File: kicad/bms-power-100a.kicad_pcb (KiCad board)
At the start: 4 copper layers, 120 x 65 mm, 68 parts, among them J1 Conn_01x06, J2 Conn_01x06, P1 CONN_01X01, P2 CONN_01X01, P3 CONN_01X01, P4 CONN_01X01, Q1 IPT015N10N5, Q10 BSS123N, Q2 IPT015N10N5, Q21 ZXMP6A13F, Q3 IPT015N10N5, Q4 IPT015N10N5, Q5 IPT015N10N5, Q6 IPT015N10N5, Q7 IPT015N10N5, Q8 IPT015N10N5, Q9 DMG1013UW

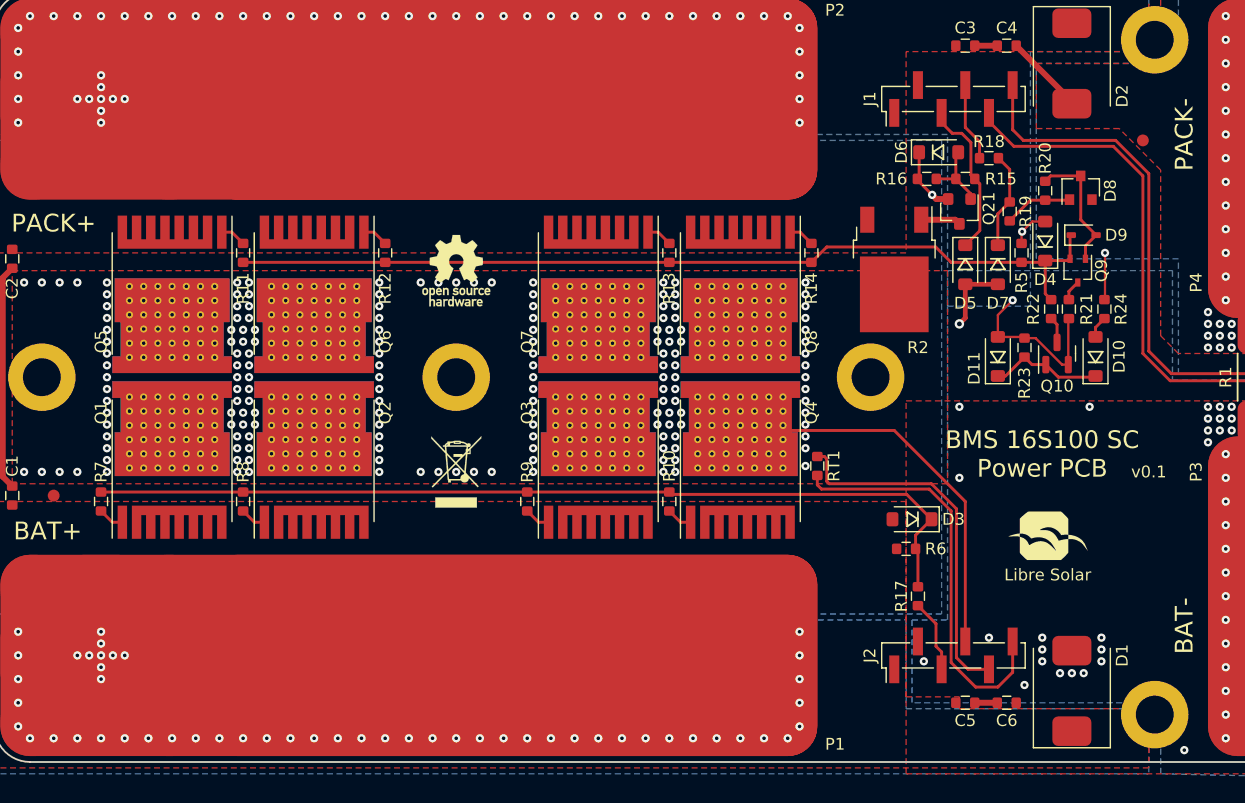
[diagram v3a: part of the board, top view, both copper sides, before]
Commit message: Updates based on review comments (v0.2)
This is the design revision that was ordered for the first prototype build.

The pinout of the cell connector and the board-to-board connector changed
compared to v0.1, hence it got a minor revision update.

The control board is now a 4-layer board to improve the grounding of the
PCB. Various other suggested improvements from the design review are also
included in this update.

Fixes #11, #12, #13, #17, #18, #19
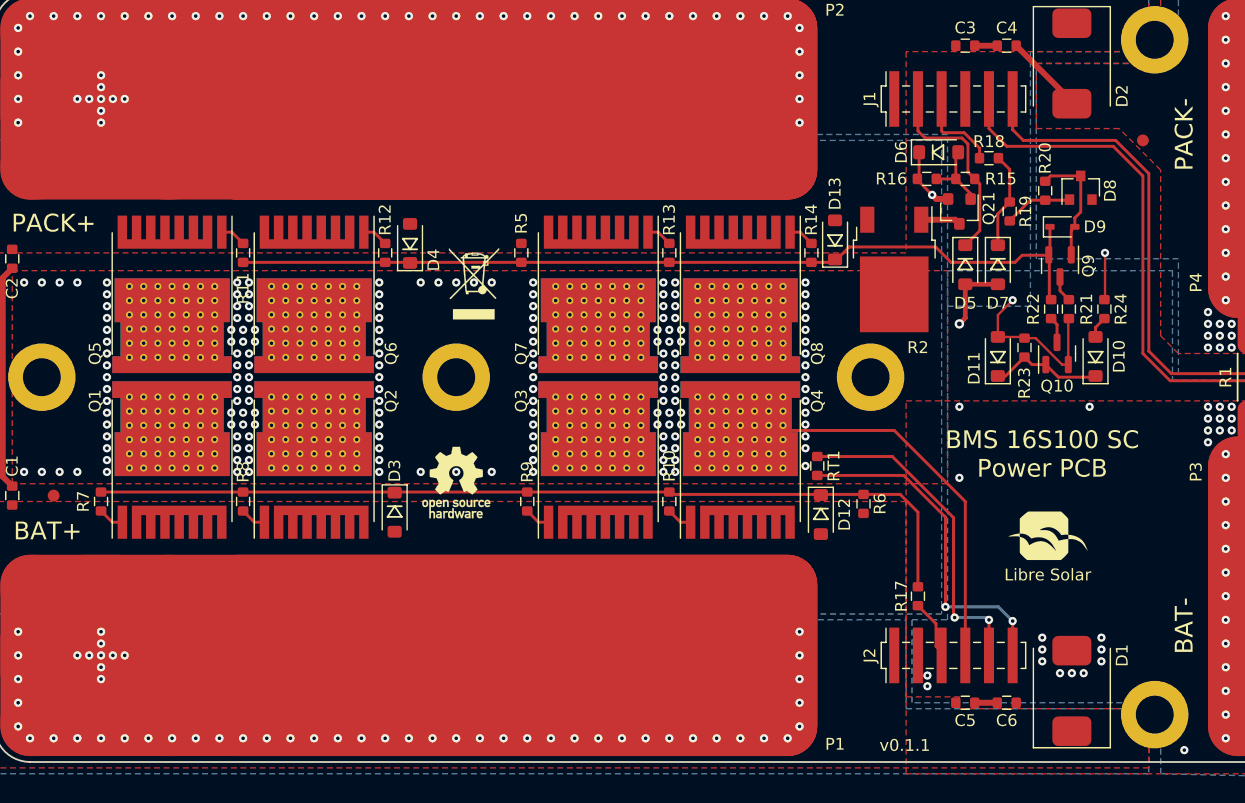
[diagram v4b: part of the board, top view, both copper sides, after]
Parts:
- added D12: 16V, LibreSolar:D_SOD-123, F.Cu at (149.8, 99.1)
- added D13: 16V, LibreSolar:D_SOD-123, F.Cu at (151.0, 75.9)
- J1, J2: footprint Connector_PinHeader_2.00mm:PinHeader_1x06_P2.00mm_Vertical_SMD_Pin1Left -> LibreSolar:PinHeader_1x06_P2.00mm_Vertical_SMD
- Q9: value DMG1013UW -> MMBT3906; footprint Package_TO_SOT_SMD:SOT-323_SC-70 -> Package_TO_SOT_SMD:SOT-23
- R10, R11, R12, R13, R14, R7, R8, R9: value 51 -> 47
- R20: value 56k -> 68k
- moved D4 53.7 mm to (115.1, 76.2)
- moved D3 43.7 mm to (113.8, 98.9), turned to -90 degrees
- moved R5 42.2 mm to (124.5, 77.0)
- moved LOGO1 17.9 mm to (119.0, 96.4)
- moved REF** 16.0 mm to (120.5, 79.6)
- moved R6 5.23 mm to (153.4, 98.2), turned to -90 degrees
- moved D9 1.93 mm to (170.2, 74.8)
- moved Q9 1.55 mm to (170.0, 78.1)
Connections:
- J1 pad 2: unconnected-(J1-Pad2) -> /PDSG
- J1 pad 3: /PDSG -> /DSG
- J1 pad 4: /DSG -> unconnected-(J1-Pad4)
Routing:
- net Net-(J2-Pad6): track 35.0 -> 28.9 mm, vias 0 -> 2
- net /PDSG: track 13.5 -> 18.0 mm
- net /PACK+: track 17.8 -> 14.4 mm, vias 54 -> 53
- net Net-(J2-Pad5): track 30.4 -> 28.1 mm, vias 0 -> 2
- net /CHG: track 6.20 -> 4.74 mm
- net /CHG_G: track 77.4 -> 76.0 mm
- net /DSG_G: track 76.6 -> 75.7 mm
- net Net-(D8-Pad1): track 11.1 -> 10.2 mm
- net GND: track 51.8 -> 52.2 mm, vias 98 -> 97
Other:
- board text added: "v0.1.1"
- board text removed: "v0.1"
